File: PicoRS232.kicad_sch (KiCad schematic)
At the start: 25 parts, among them J1 RS232_0, J2 RS232_0, J3 RS232_0, J4 RS232_0, J5 RS232_0, J6 RS232_0, U1 MAX3232CDR, U2 MAX3232CDR, U3 MAX3232CDR

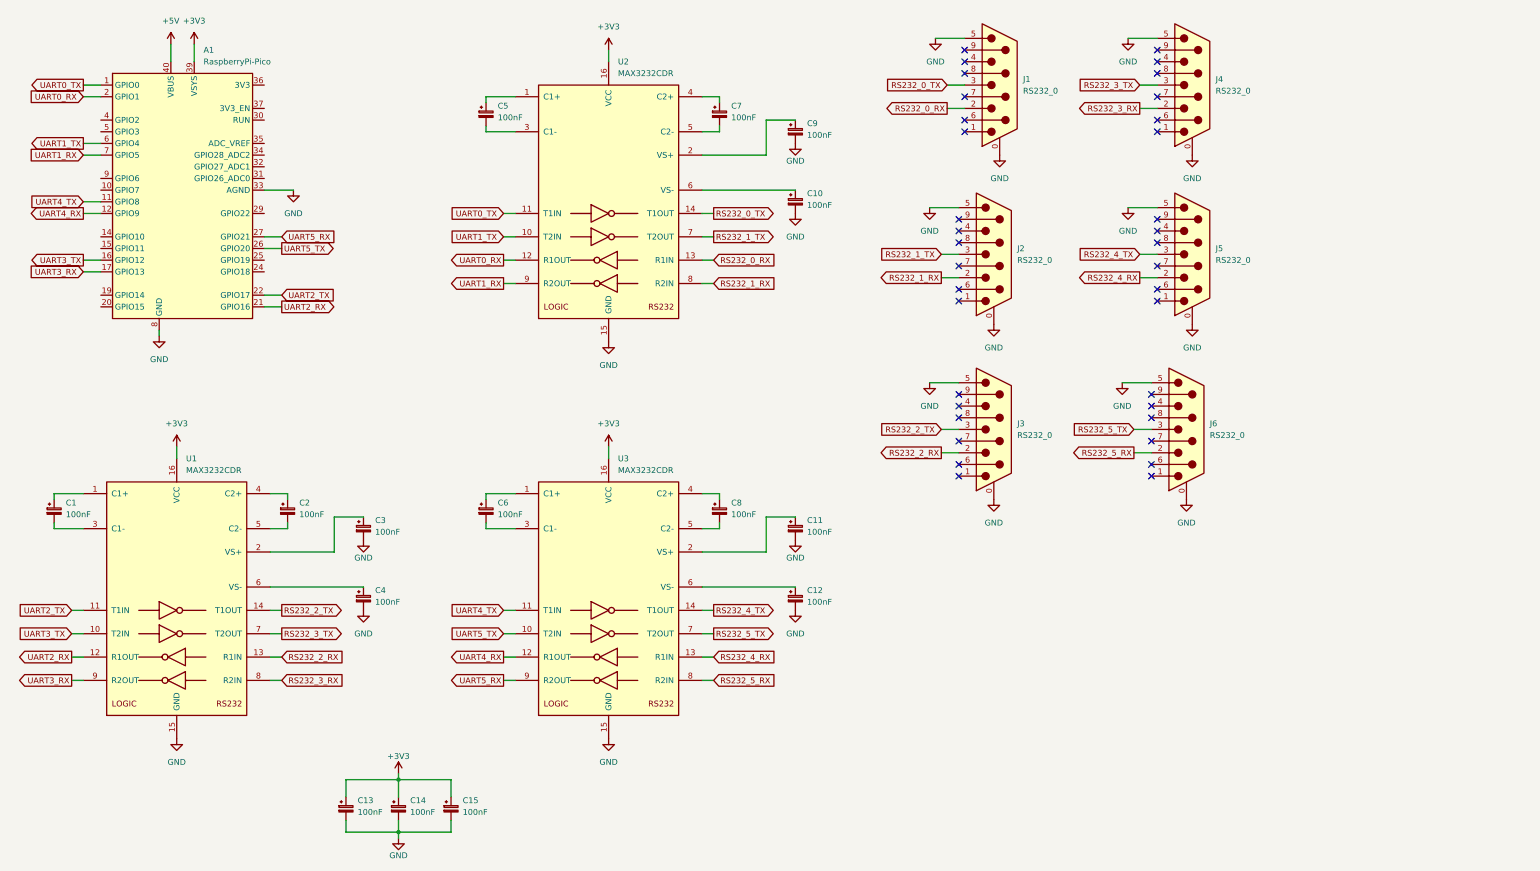
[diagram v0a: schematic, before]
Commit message: Break out unused GPIO pins to headers.
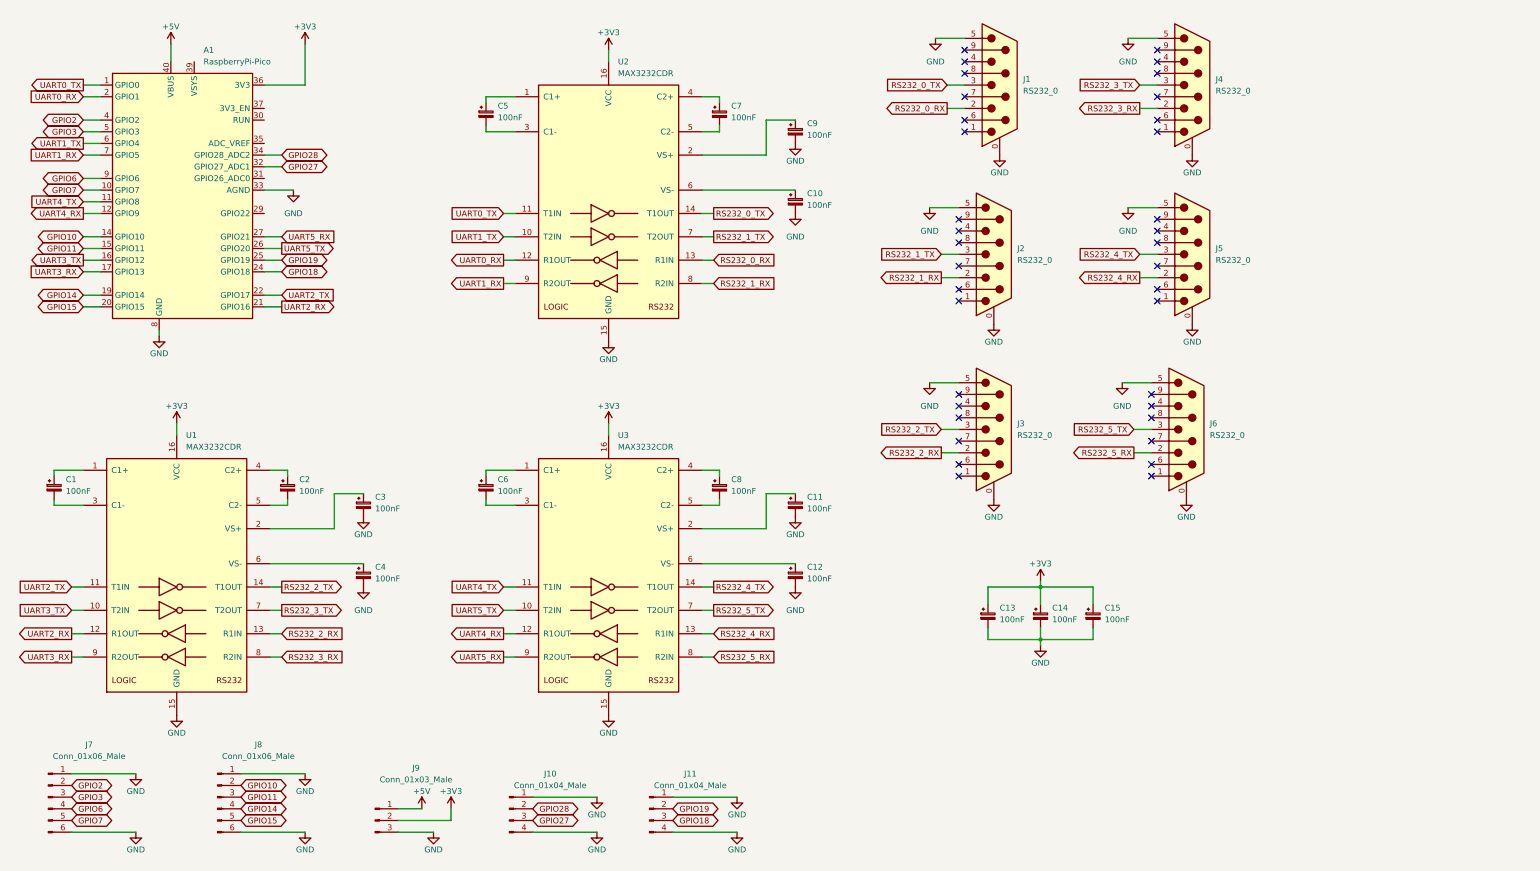
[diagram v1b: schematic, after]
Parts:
- added J10, J11: Conn_01x04_Male, Connector_PinHeader_2.54mm:PinHeader_1x04_P2.54mm_Vertical, symbol Connector:Conn_01x04_Male
- added J7, J8: Conn_01x06_Male, Connector_PinHeader_2.54mm:PinHeader_1x06_P2.54mm_Vertical, symbol Connector:Conn_01x06_Male
- added J9: Conn_01x03_Male, Connector_PinHeader_2.54mm:PinHeader_1x03_P2.54mm_Vertical, symbol Connector:Conn_01x03_Male
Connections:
- net +3V3: now also A1.36 (3V3), J9.2 (Pin_2); no longer A1.39 (VSYS)
- net +5V: now also J9.1 (Pin_1)
- net GND: now also J10.1 (Pin_1), J10.4 (Pin_4), J11.1 (Pin_1), J11.4 (Pin_4), J7.1 (Pin_1), J7.6 (Pin_6), J8.1 (Pin_1), J8.6 (Pin_6), J9.3 (Pin_3)
- net GPIO7: now reaches A1.10 (GPIO7)
- net GPIO7: now also J7.5 (Pin_5)
- net GPIO10: now reaches A1.14 (GPIO10)
- net GPIO10: now also J8.2 (Pin_2)
- net GPIO11: now reaches A1.15 (GPIO11)
- net GPIO11: now also J8.3 (Pin_3)
- net GPIO14: now reaches A1.19 (GPIO14)
- net GPIO14: now also J8.4 (Pin_4)
- net GPIO15: now reaches A1.20 (GPIO15)
- net GPIO15: now also J8.5 (Pin_5)
- net GPIO18: now reaches A1.24 (GPIO18)
- net GPIO18: now also J11.3 (Pin_3)
- net GPIO19: now reaches A1.25 (GPIO19)
- net GPIO19: now also J11.2 (Pin_2)
- net GPIO27: now reaches A1.32 (GPIO27_ADC1)
- net GPIO27: now also J10.3 (Pin_3)
- net GPIO28: now reaches A1.34 (GPIO28_ADC2)
- net GPIO28: now also J10.2 (Pin_2)
- net GPIO2: now reaches A1.4 (GPIO2)
- net GPIO2: now also J7.2 (Pin_2)
- net GPIO3: now reaches A1.5 (GPIO3)
- net GPIO3: now also J7.3 (Pin_3)
- net GPIO6: now reaches A1.9 (GPIO6)
- net GPIO6: now also J7.4 (Pin_4)
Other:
- moved on the sheet: C1, C11, C12, C13, C14, C15, C2, C3, C4, C6, C8, U1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

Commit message: Organize schematic and add mounting holes.
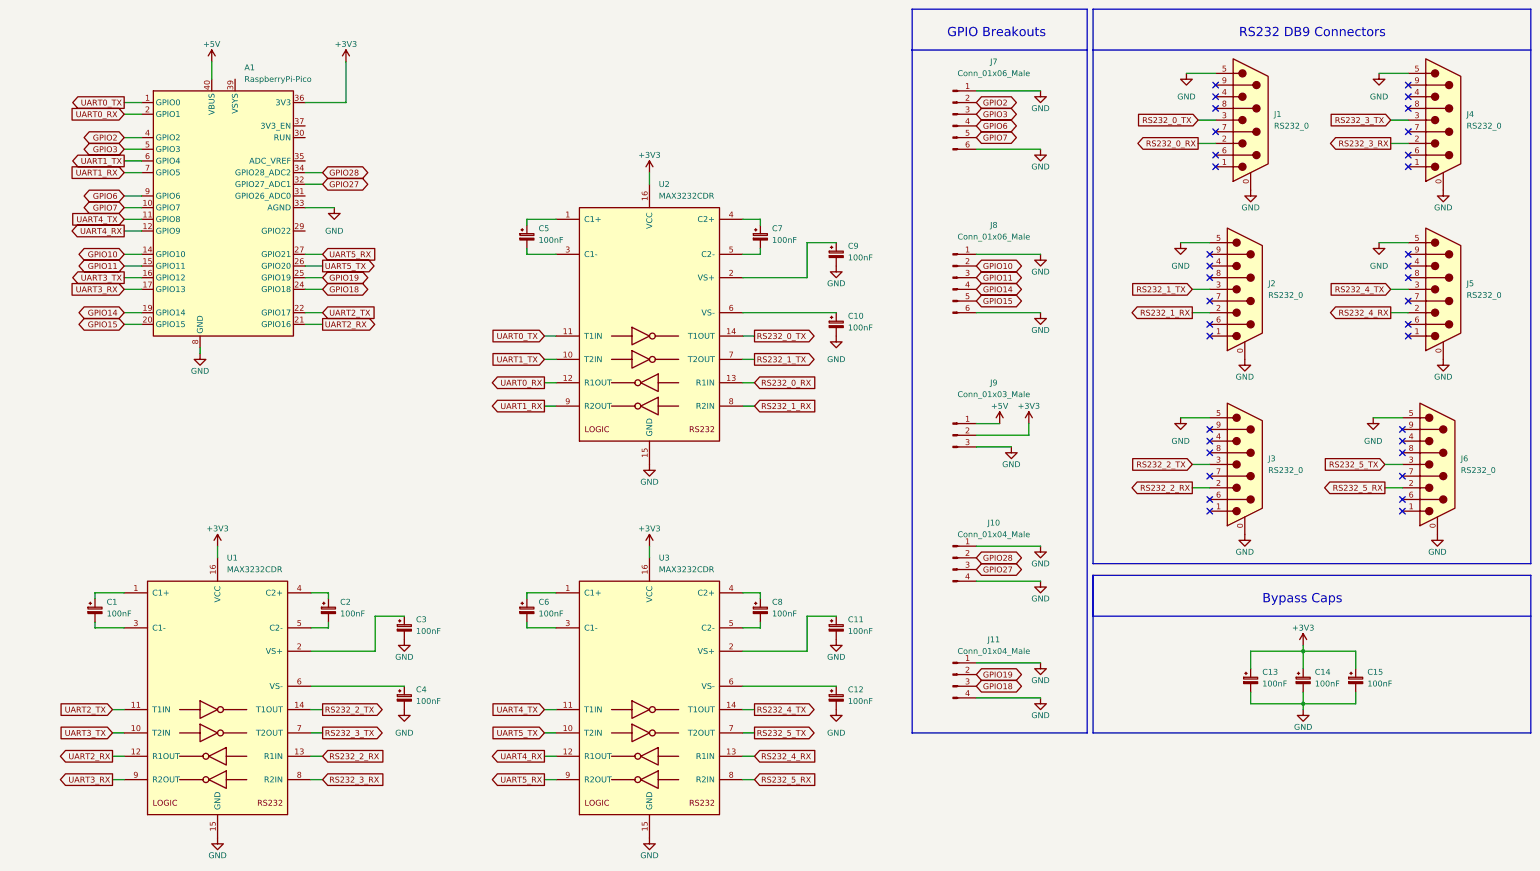
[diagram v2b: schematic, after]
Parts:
- J10: now in the parts list
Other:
- note added: "Bypass Caps"
- note added: "GPIO Breakouts"
- note added: "RS232 DB9 Connectors"
- moved on the sheet: A1, C1, C10, C11, C12, C13, C14, C15, C2, C3, C4, C5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

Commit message: Add a reset button and merge two pin headers.
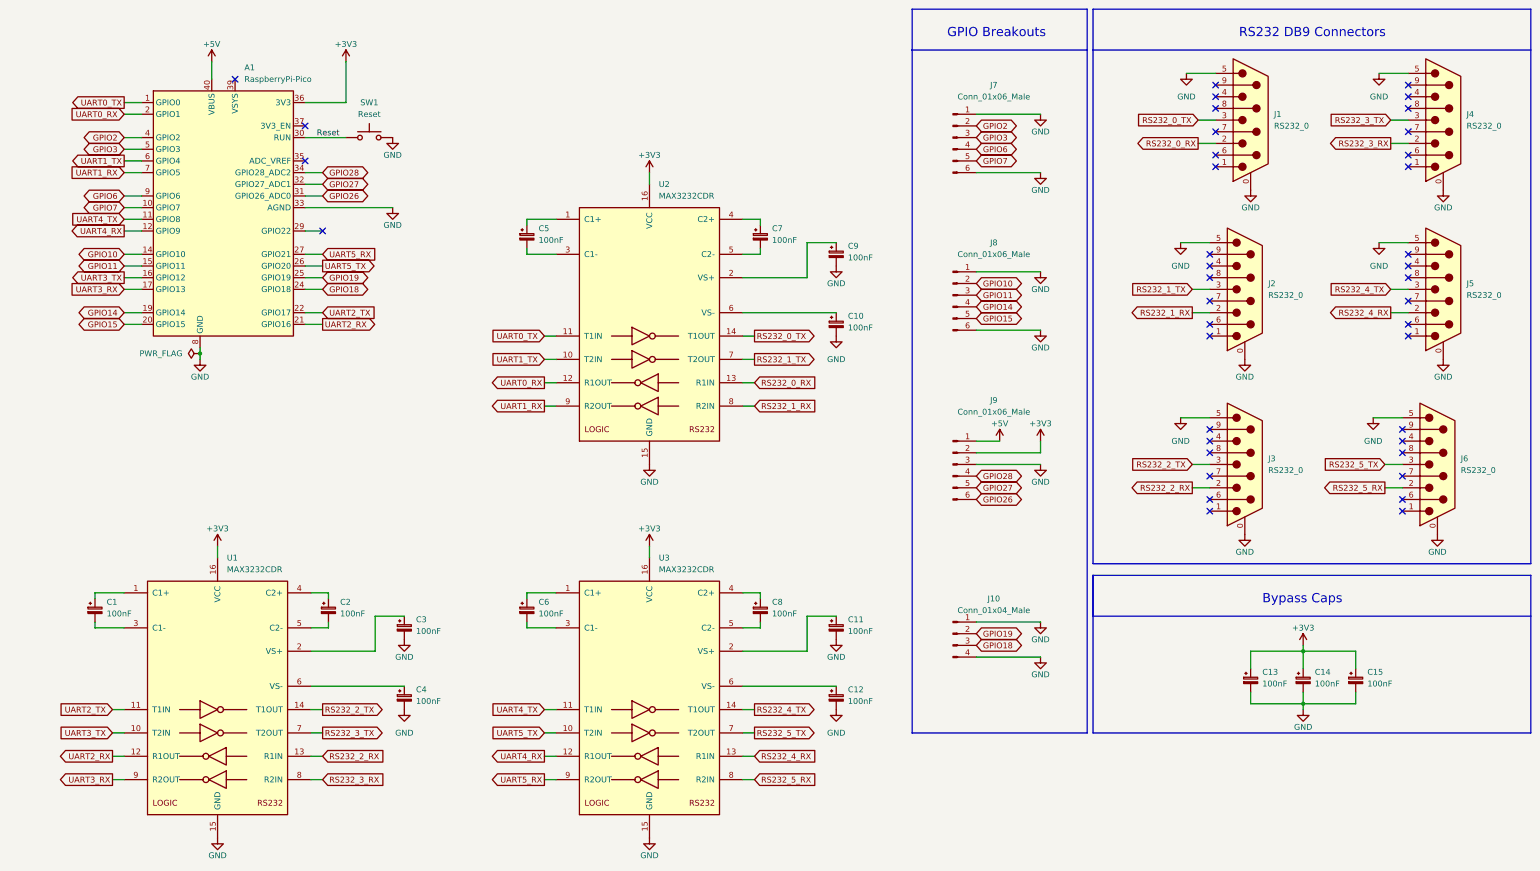
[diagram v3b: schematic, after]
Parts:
- removed J10: Conn_01x04_Male, Connector_PinHeader_2.54mm:PinHeader_1x04_P2.54mm_Vertical, symbol Connector:Conn_01x04_Male
- removed J9: Conn_01x03_Male, Connector_PinHeader_2.54mm:PinHeader_1x03_P2.54mm_Vertical, symbol Connector:Conn_01x03_Male
- added J9: Conn_01x06_Male, Connector_PinHeader_2.54mm:PinHeader_1x06_P2.54mm_Vertical, symbol Connector:Conn_01x06_Male
- added SW1: Reset, Button_Switch_SMD:SW_SPST_PTS810, symbol Switch:SW_Push
- renumbered J11 to J10
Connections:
- net +3V3: now also J9.2 (Pin_2)
- net +5V: now also J9.1 (Pin_1)
- net GND: now also J9.3 (Pin_3), SW1.2
- net GPIO27: now also J9.5 (Pin_5)
- net GPIO28: now also J9.4 (Pin_4)
- net Reset: now reaches A1.30 (RUN)
- net Reset: now also SW1.1
- net GPIO26: now reaches A1.31 (GPIO26_ADC0)
- net GPIO26: now also J9.6 (Pin_6)
- no-connect marks 36 -> 40
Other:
- moved on the sheet: J10, J7, J8

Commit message: Change reset button to one JLCPCB has in stock.
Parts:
- SW1: footprint Button_Switch_SMD:SW_SPST_PTS810 -> Button_Switch_SMD:SW_SPST_SKQG_WithStem; LCSC (none) -> C318889; now in the parts list
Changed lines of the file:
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@@
   )
   (symbol (lib_id "Switch:SW_Push") (at 88.9 40.64 0) (unit 1)
-    (in_bom no) (on_board yes)
+    (in_bom yes) (on_board yes)
     (property "Reference" "SW1" (id 0) (at 88.9 33.02 0))
     (property "Value" "Reset" (id 1) (at 88.9 35.56 0))
-    (property "Footprint" "Button_Switch_SMD:SW_SPST_PTS810" (id 2) (at 88.9 35.56 0)
+    (property "Footprint" "Button_Switch_SMD:SW_SPST_SKQG_WithStem" (id 2) (at 88.9 35.56 0)
       (effects (font (size 1.27 1.27)) hide)
     )
     (property "Datasheet" "~" (id 3) (at 88.9 35.56 0)
+      (effects (font (size 1.27 1.27)) hide)
+    )
+    (property "LCSC" "C318889" (id 4) (at 88.9 40.64 0)
       (effects (font (size 1.27 1.27)) hide)
     )
@@
     )
     (path "/098245f6-d289-4dd8-9a04-b85a1d0fb09a"
-      (reference "SW1") (unit 1) (value "Reset") (footprint "Button_Switch_SMD:SW_SPST_PTS810")
+      (reference "SW1") (unit 1) (value "Reset") (footprint "Button_Switch_SMD:SW_SPST_SKQG_WithStem")
     )
     (path "/d7189430-dc2f-47a9-b6d6-7ea28845876a"

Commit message: Add silkscreen with name, version, and url.
Also, add pin header part numbers, but leave them out of the BOM.
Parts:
- J10: LCSC (none) -> C225479
- J7, J8, J9: LCSC (none) -> C225481
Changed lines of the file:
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@@
+      (effects (font (size 1.27 1.27)) hide)
+    )
+    (property "LCSC" "C225481" (id 4) (at 215.9 111.76 0)
       (effects (font (size 1.27 1.27)) hide)
     )
@@
     )
     (property "Datasheet" "~" (id 3) (at 215.9 74.93 0)
+      (effects (font (size 1.27 1.27)) hide)
+    )
+    (property "LCSC" "C225481" (id 4) (at 215.9 74.93 0)
       (effects (font (size 1.27 1.27)) hide)
     )
@@
       (effects (font (size 1.27 1.27)) hide)
     )
+    (property "LCSC" "C225479" (id 4) (at 215.9 148.59 0)
+      (effects (font (size 1.27 1.27)) hide)
+    )
     (pin "1")
     (pin "2")
@@
       (effects (font (size 1.27 1.27)) hide)
     )
+    (property "LCSC" "C225481" (id 4) (at 215.9 40.64 0)
+      (effects (font (size 1.27 1.27)) hide)
+    )
